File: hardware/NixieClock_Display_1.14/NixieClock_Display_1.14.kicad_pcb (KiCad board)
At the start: 2 copper layers, 17.5 x 41.9 mm, 2 parts, among them J1 Conn_01x08, J2 Conn_01x08

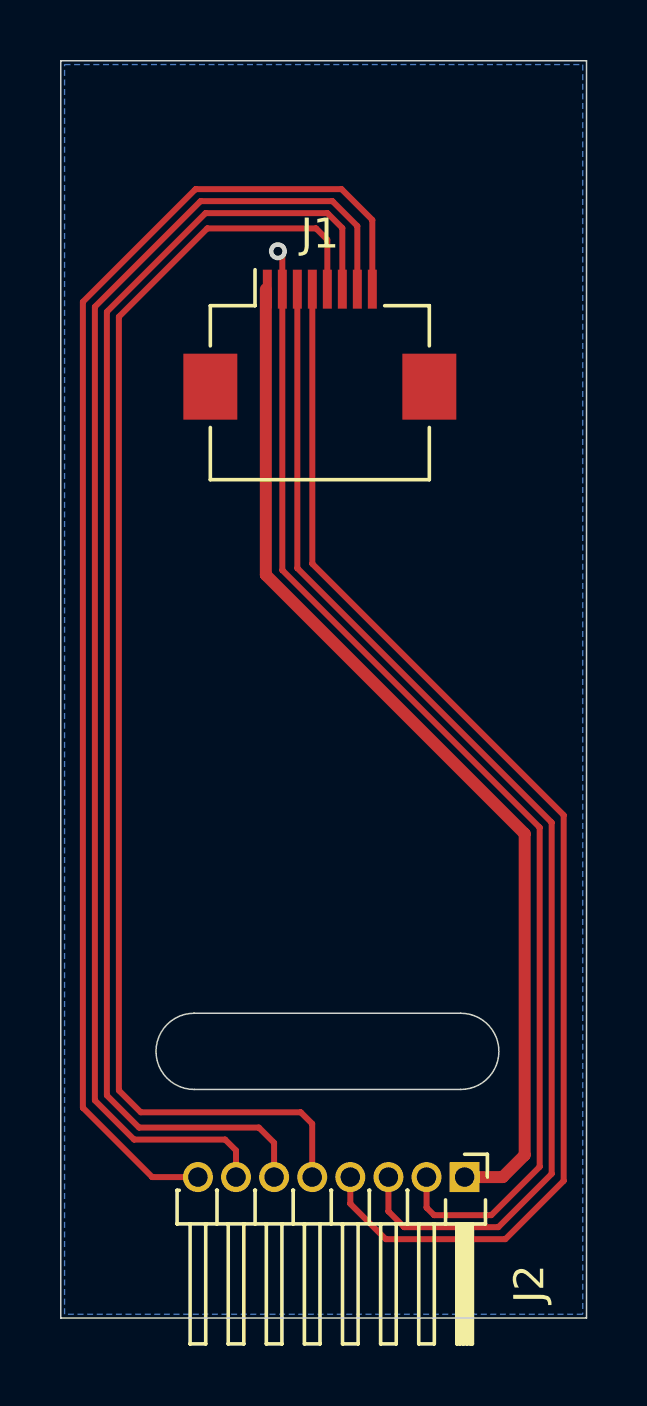
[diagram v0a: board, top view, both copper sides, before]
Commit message: update pcb. distance between fpc-connector corrected
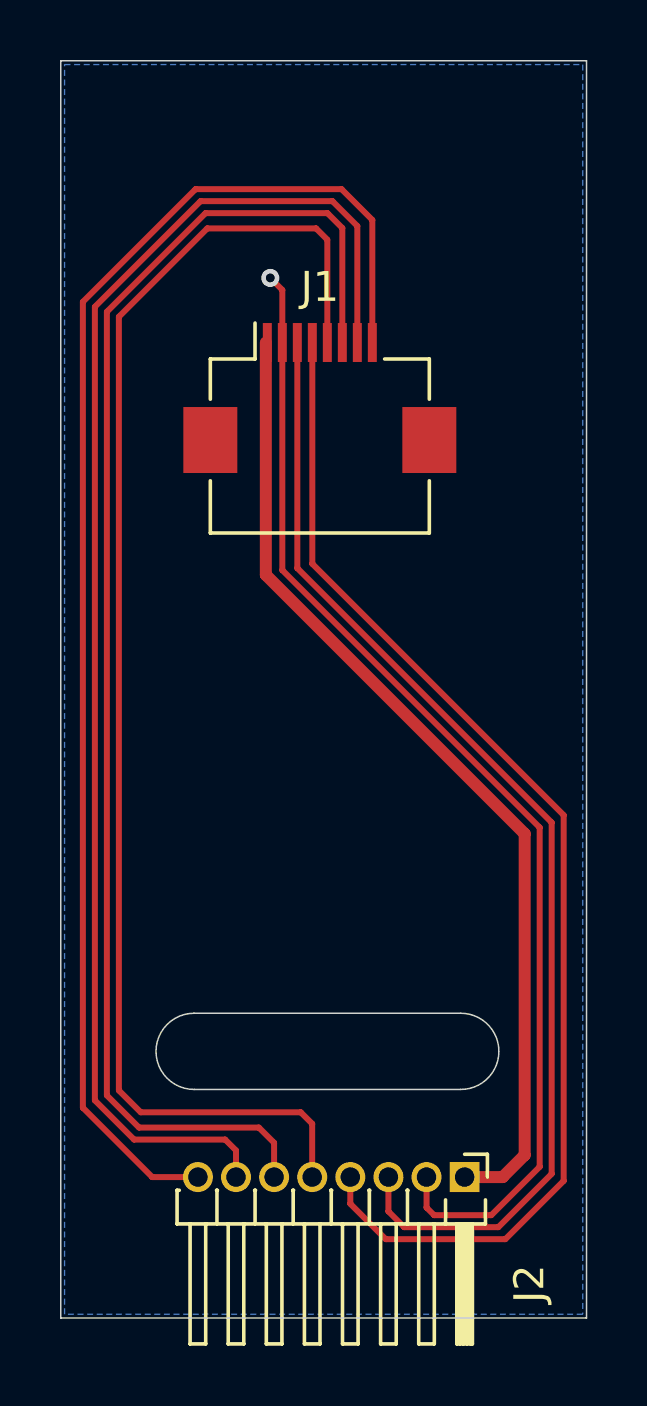
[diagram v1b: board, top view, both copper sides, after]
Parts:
- moved J1 1.78 mm to (135.6, 72.2)
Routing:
- net /LEDA: track 34.7 -> 33.0 mm
- net /RS: track 42.5 -> 41.2 mm
- net /SDA: track 44.4 -> 45.7 mm
- net /SCL: track 44.9 -> 46.2 mm
- net /RESET: track 40.5 -> 39.3 mm
- net /VDD: track 45.4 -> 46.7 mm
- net /CS: track 45.6 -> 46.9 mm
- net /GND: track 39.9 -> 38.9 mm
